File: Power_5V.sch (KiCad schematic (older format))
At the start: 7 parts

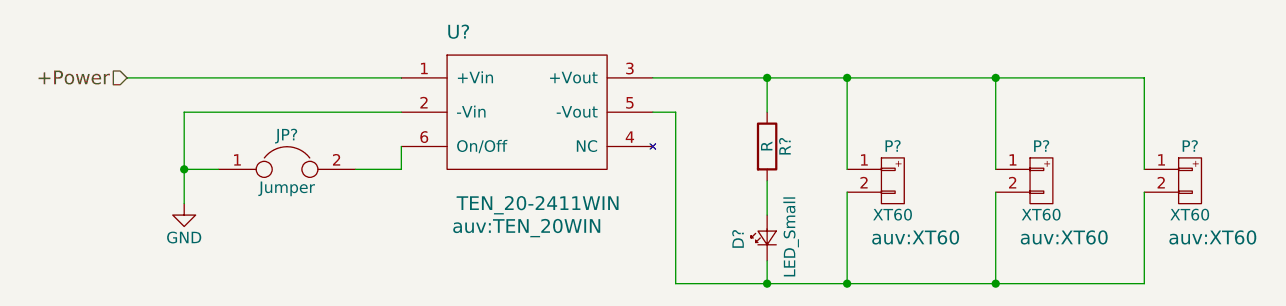
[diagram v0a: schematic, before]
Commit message: assign component value and change BC847B to BC817-40
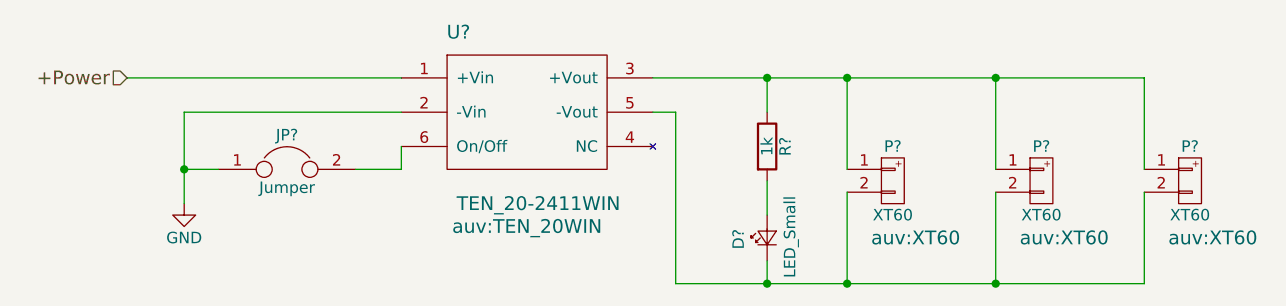
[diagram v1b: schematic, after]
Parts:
- R?: value R -> 1k
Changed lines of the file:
@@
 P 6600 3450
 F 0 "R?" V 6680 3450 50  0000 C CNN
-F 1 "R" V 6600 3450 50  0000 C CNN
+F 1 "1k" V 6600 3450 50  0000 C CNN
 F 2 "Resistors_SMD:R_0603" V 6530 3450 50  0001 C CNN
 F 3 "" H 6600 3450 50  0001 C CNN
